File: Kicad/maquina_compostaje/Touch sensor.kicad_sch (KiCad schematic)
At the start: 1 part, among them J5 Conn_01x03

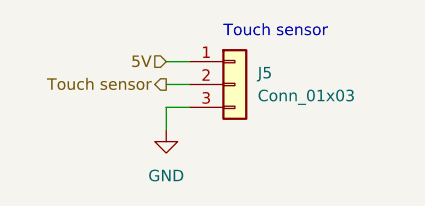
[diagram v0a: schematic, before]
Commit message: se agregaron componentes en la parte inferior de la placa
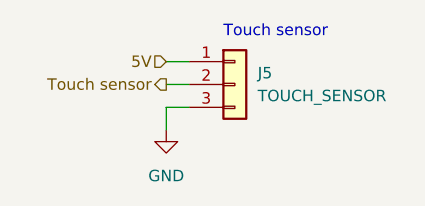
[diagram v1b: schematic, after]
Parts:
- J5: value Conn_01x03 -> TOUCH_SENSOR
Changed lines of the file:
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@@
       (effects (font (size 1.27 1.27)) (justify left))
     )
-    (property "Value" "Conn_01x03" (id 1) (at 38.1 30.4799 0)
+    (property "Value" "TOUCH_SENSOR" (id 1) (at 38.1 30.4799 0)
       (effects (font (size 1.27 1.27)) (justify left))
     )
